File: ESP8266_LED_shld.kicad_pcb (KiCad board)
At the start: 2 copper layers, 59.1 x 52.7 mm, 28 parts, among them J1 Pwr_Dat_Out, J2 CONN_02X08, J3 CONN_DIN, J4 BARREL_JACK, J5 USB-MICROB, J6 CONN_01X06, M1 LOGIC_LEVEL_CONVERTER, T1 Test_Point_2Pads, U1 ESP-07v2, U2 AMS1117

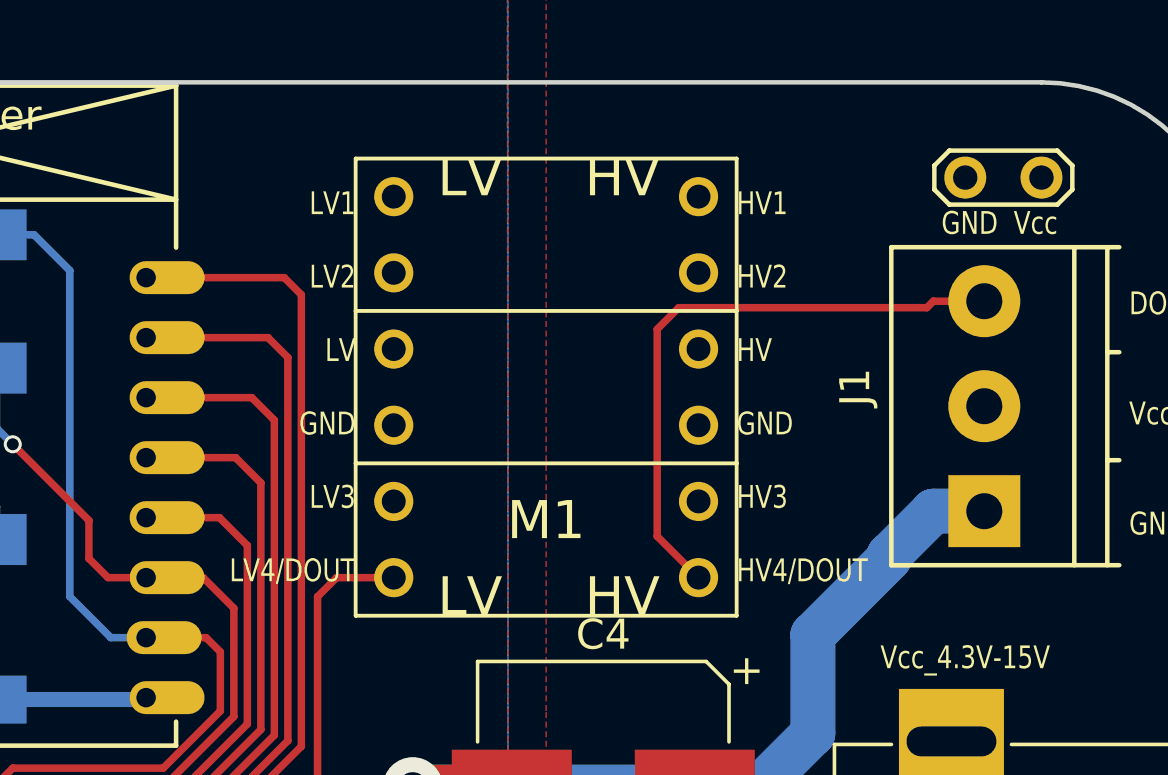
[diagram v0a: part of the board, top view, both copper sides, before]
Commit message: added resistor between DOUT and HV4 to protect data pin of LED stip and fixed some silk screen labels (positions)
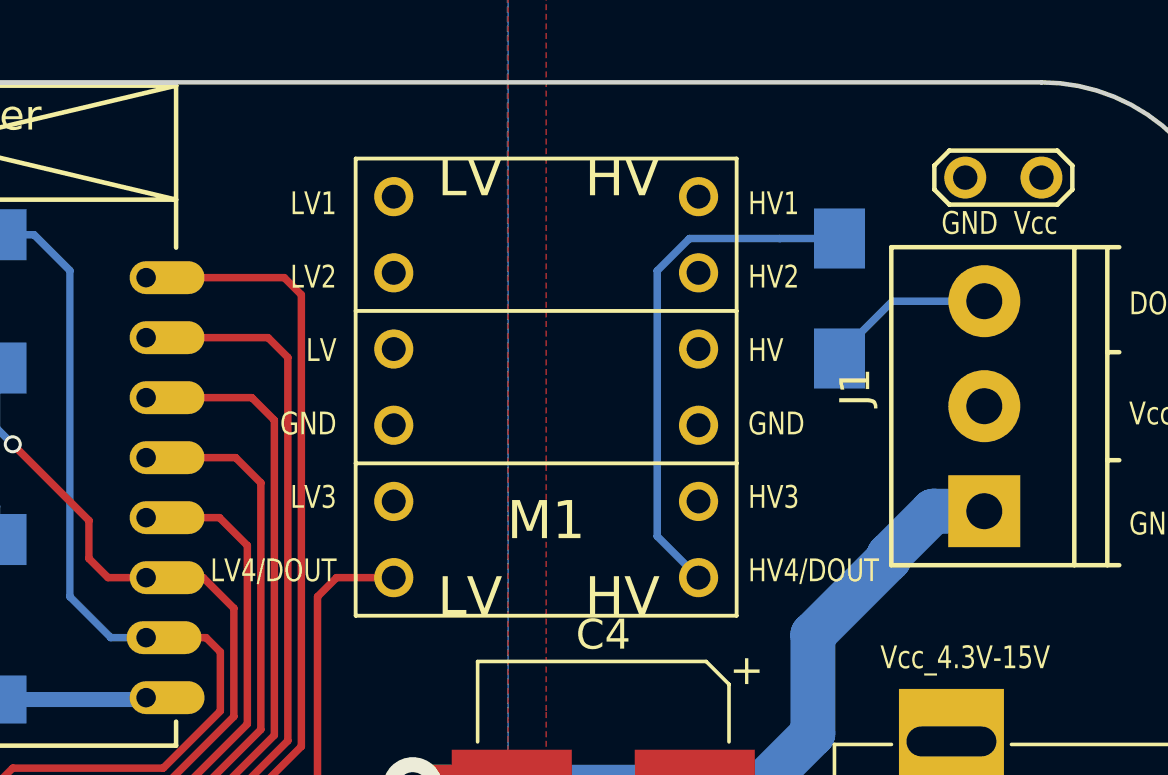
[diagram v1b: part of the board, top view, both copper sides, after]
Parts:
- added R7: 1K, Resistors_SMD:R_1206_HandSoldering, B.Cu at (204.7, 87.9)
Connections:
- M1 pad P$7: DOUT -> Net-(M1-PadP$7)
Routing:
- net Net-(M1-PadP$7): track 0.00 -> 17.3 mm
- net DOUT: track 20.5 -> 6.02 mm
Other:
- board text added: "Revision 1.1 Vcc: 4.3V-15V, 8A (PCB) +3V3: 800mA USB+DC_JACK=USB_GND_BRK USB+Vcc=NO BRK!"
- board text removed: "Revision 1.0 Vcc: 4.3V-15V, 8A (PCB) +3V3: 800mA USB+DC_JACK=USB_GND_BRK USB+Vcc=NO BRK!"
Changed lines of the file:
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@@
 (kicad_pcb (version 4) (host pcbnew 4.0.6)
   (general
-    (links 71)
-    (no_connects 3)
+    (links 72)
+    (no_connects 5)
     (area 158.674999 80.569999 217.880001 133.425001)
     (thickness 1.6)
     (drawings 27)
-    (tracks 248)
+    (tracks 250)
     (zones 0)
-    (modules 28)
-    (nets 33)
+    (modules 29)
+    (nets 34)
   )
   (page A4)
@@
   (net 31 /DTR)
   (net 32 /CTS)
+  (net 33 "Net-(M1-PadP$7)")
   (net_class Default "This is the default net class."
     (clearance 0.2)
@@
     (add_net "Net-(M1-PadP$2)")
     (add_net "Net-(M1-PadP$5)")
+    (add_net "Net-(M1-PadP$7)")
     (add_net "Net-(M1-PadP$8)")
     (add_net REST)
@@
       (net 4 DIN))
     (pad P$7 thru_hole circle (at 11.43 -1.27) (size 1.30556 1.30556) (drill 0.79756) (layers *.Cu *.Mask F.SilkS)
-      (net 3 DOUT))
+      (net 33 "Net-(M1-PadP$7)"))
     (pad P$8 thru_hole circle (at 11.43 -3.81) (size 1.30556 1.30556) (drill 0.79756) (layers *.Cu *.Mask F.SilkS)
       (net 23 "Net-(M1-PadP$8)"))
@@
       (net 25 "Net-(M1-PadP$12)"))
   )
+  (module Resistors_SMD:R_1206_HandSoldering (layer B.Cu)
+    (at 204.724 87.852 270)
+    (descr "Resistor SMD 1206, hand soldering")
+    (tags "resistor 1206")
+    (attr smd)
+    (fp_text reference R7 (at 0 1.85 270) (layer B.SilkS)
+      (effects (font (size 1 1) (thickness 0.15)) (justify mirror))
+    )
+    (fp_text value 1K (at 0 -1.9 270) (layer B.Fab)
+      (effects (font (size 1 1) (thickness 0.15)) (justify mirror))
+    )
+    (fp_text user %R (at 0 0 270) (layer B.Fab)
+      (effects (font (size 0.7 0.7) (thickness 0.105)) (justify mirror))
+    )
+    (fp_line (start -1.6 -0.8) (end -1.6 0.8) (layer B.Fab) (width 0.1))
+    (fp_line (start 1.6 -0.8) (end -1.6 -0.8) (layer B.Fab) (width 0.1))
+    (fp_line (start 1.6 0.8) (end 1.6 -0.8) (layer B.Fab) (width 0.1))
+    (fp_line (start -1.6 0.8) (end 1.6 0.8) (layer B.Fab) (width 0.1))
+    (fp_line (start 1 -1.07) (end -1 -1.07) (layer B.SilkS) (width 0.12))
+    (fp_line (start -1 1.07) (end 1 1.07) (layer B.SilkS) (width 0.12))
+    (fp_line (start -3.25 1.11) (end 3.25 1.11) (layer B.CrtYd) (width 0.05))
+    (fp_line (start -3.25 1.11) (end -3.25 -1.1) (layer B.CrtYd) (width 0.05))
+    (fp_line (start 3.25 -1.1) (end 3.25 1.11) (layer B.CrtYd) (width 0.05))
+    (fp_line (start 3.25 -1.1) (end -3.25 -1.1) (layer B.CrtYd) (width 0.05))
+    (pad 1 smd rect (at -2 0 270) (size 2 1.7) (layers B.Cu B.Paste B.Mask)
+      (net 33 "Net-(M1-PadP$7)"))
+    (pad 2 smd rect (at 2 0 270) (size 2 1.7) (layers B.Cu B.Paste B.Mask)
+      (net 3 DOUT))
+    (model ${KISYS3DMOD}/Resistors_SMD.3dshapes/R_1206.wrl
+      (at (xyz 0 0 0))
+      (scale (xyz 1 1 1))
+      (rotate (xyz 0 0 0))
+    )
+  )
   (gr_text "EN\n\n\n\nDIS" (at 163.322 124.46) (layer F.SilkS)
     (effects (font (size 0.76 0.6) (thickness 0.125)) (justify left))
@@
     (effects (font (size 0.76 0.6) (thickness 0.125)) (justify left))
   )
-  (gr_text "Revision 1.0\n\nVcc: 4.3V-15V, 8A (PCB)    +3V3: 800mA    \nUSB+DC_JACK=USB_GND_BRK\nUSB+Vcc=NO BRK!" (at 202.565 105.41) (layer B.SilkS)
+  (gr_text "Revision 1.1\n\nVcc: 4.3V-15V, 8A (PCB)    +3V3: 800mA    \nUSB+DC_JACK=USB_GND_BRK\nUSB+Vcc=NO BRK!" (at 202.565 105.41) (layer B.SilkS)
     (effects (font (size 0.9 0.9) (thickness 0.2)) (justify left mirror))
   )
@@
     (effects (font (size 0.76 0.6) (thickness 0.125)) (justify left))
   )
-  (gr_text "LV1\n\nLV2\n\nLV\n\nGND\n\nLV3\n\nLV4/DOUT" (at 188.595 90.805) (layer F.SilkS)
+  (gr_text "LV1\n\nLV2\n\nLV\n\nGND\n\nLV3\n\nLV4/DOUT" (at 187.96 90.805) (layer F.SilkS)
     (effects (font (size 0.76 0.6) (thickness 0.125)) (justify right))
   )
-  (gr_text "HV1\n\nHV2\n\nHV\n\nGND\n\nHV3\n\nHV4/DOUT" (at 201.295 90.805) (layer F.SilkS)
+  (gr_text "HV1\n\nHV2\n\nHV\n\nGND\n\nHV3\n\nHV4/DOUT" (at 201.676 90.805) (layer F.SilkS)
     (effects (font (size 0.76 0.6) (thickness 0.125)) (justify left))
   )
@@
   (segment (start 181.61 101.155) (end 181.546 101.219) (width 0.5) (layer B.Cu) (net 2))
   (segment (start 181.546 101.219) (end 176.625 101.219) (width 0.5) (layer B.Cu) (net 2))
-  (segment (start 200.025 97.155) (end 198.647219 95.777219) (width 0.25) (layer F.Cu) (net 3))
-  (segment (start 198.647219 95.777219) (end 198.647219 88.873664) (width 0.25) (layer F.Cu) (net 3))
-  (segment (start 198.647219 88.873664) (end 199.363664 88.157219) (width 0.25) (layer F.Cu) (net 3))
-  (segment (start 207.852944 87.94) (end 209.55 87.94) (width 0.25) (layer F.Cu) (net 3))
-  (segment (start 199.363664 88.157219) (end 207.635725 88.157219) (width 0.25) (layer F.Cu) (net 3))
-  (segment (start 207.635725 88.157219) (end 207.852944 87.94) (width 0.25) (layer F.Cu) (net 3))
+  (segment (start 209.55 87.94) (end 206.486 87.94) (width 0.25) (layer B.Cu) (net 3))
+  (segment (start 206.486 87.94) (end 204.724 89.702) (width 0.25) (layer B.Cu) (net 3))
+  (segment (start 204.724 89.702) (end 204.724 89.852) (width 0.25) (layer B.Cu) (net 3))
   (segment (start 209.24 87.94) (end 209.55 87.94) (width 0.25) (layer F.Cu) (net 3))
   (segment (start 189.865 97.155) (end 187.96 97.155) (width 0.25) (layer F.Cu) (net 4))
@@
   (segment (start 210.15706 125.75794) (end 210.185 125.73) (width 0.25) (layer F.Cu) (net 30))
   (segment (start 208.915 124.46) (end 208.915 123.17) (width 0.25) (layer B.Cu) (net 30))
+  (segment (start 202.735 85.852) (end 204.724 85.852) (width 0.25) (layer B.Cu) (net 33))
+  (segment (start 200.025 97.155) (end 198.647219 95.777219) (width 0.25) (layer B.Cu) (net 33))
+  (segment (start 198.647219 95.777219) (end 198.647219 86.925664) (width 0.25) (layer B.Cu) (net 33))
+  (segment (start 198.647219 86.925664) (end 199.720883 85.852) (width 0.25) (layer B.Cu) (net 33))
+  (segment (start 199.720883 85.852) (end 202.735 85.852) (width 0.25) (layer B.Cu) (net 33))
   (zone (net 0) (net_name "") (layer B.Cu) (hatch edge 0.508)
     (connect_pads (clearance 0.508))

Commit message: updated PCB design
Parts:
- D2: footprint Diodes_SMD:D_SOD-323_HandSoldering -> Diodes_SMD:D_SOD-123
- moved D2 0.13 mm to (208.8, 121.9)
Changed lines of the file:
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@@
     (thickness 1.6)
     (drawings 27)
-    (tracks 250)
+    (tracks 251)
     (zones 0)
     (modules 29)
@@
     )
   )
-  (module Diodes_SMD:D_SOD-323_HandSoldering (layer B.Cu)
-    (at 208.915 121.92 270)
-    (descr SOD-323)
-    (tags SOD-323)
-    (attr smd)
-    (fp_text reference D2 (at 0 1.85 270) (layer B.SilkS)
-      (effects (font (size 1 1) (thickness 0.15)) (justify mirror))
-    )
-    (fp_text value DIODE (at 0.1 -1.9 270) (layer B.Fab)
-      (effects (font (size 1 1) (thickness 0.15)) (justify mirror))
-    )
-    (fp_line (start -1.9 0.85) (end -1.9 -0.85) (layer B.SilkS) (width 0.12))
-    (fp_line (start 0.2 0) (end 0.45 0) (layer B.Fab) (width 0.1))
-    (fp_line (start 0.2 -0.35) (end -0.3 0) (layer B.Fab) (width 0.1))
-    (fp_line (start 0.2 0.35) (end 0.2 -0.35) (layer B.Fab) (width 0.1))
-    (fp_line (start -0.3 0) (end 0.2 0.35) (layer B.Fab) (width 0.1))
-    (fp_line (start -0.3 0) (end -0.5 0) (layer B.Fab) (width 0.1))
-    (fp_line (start -0.3 0.35) (end -0.3 -0.35) (layer B.Fab) (width 0.1))
-    (fp_line (start -0.9 -0.7) (end -0.9 0.7) (layer B.Fab) (width 0.1))
-    (fp_line (start 0.9 -0.7) (end -0.9 -0.7) (layer B.Fab) (width 0.1))
-    (fp_line (start 0.9 0.7) (end 0.9 -0.7) (layer B.Fab) (width 0.1))
-    (fp_line (start -0.9 0.7) (end 0.9 0.7) (layer B.Fab) (width 0.1))
-    (fp_line (start -2 0.95) (end 2 0.95) (layer B.CrtYd) (width 0.05))
-    (fp_line (start 2 0.95) (end 2 -0.95) (layer B.CrtYd) (width 0.05))
-    (fp_line (start -2 -0.95) (end 2 -0.95) (layer B.CrtYd) (width 0.05))
-    (fp_line (start -2 0.95) (end -2 -0.95) (layer B.CrtYd) (width 0.05))
-    (fp_line (start -1.9 -0.85) (end 1.25 -0.85) (layer B.SilkS) (width 0.12))
-    (fp_line (start -1.9 0.85) (end 1.25 0.85) (layer B.SilkS) (width 0.12))
-    (pad 1 smd rect (at -1.25 0 270) (size 1 1) (layers B.Cu B.Paste B.Mask)
-      (net 1 Vin))
-    (pad 2 smd rect (at 1.25 0 270) (size 1 1) (layers B.Cu B.Paste B.Mask)
-      (net 30 "Net-(D2-Pad2)"))
-    (model Diodes_SMD.3dshapes/D_SOD-323.wrl
-      (at (xyz 0 0 0))
-      (scale (xyz 1 1 1))
-      (rotate (xyz 0 0 180))
-    )
-  )
   (module Capacitors_SMD:CP_Elec_8x10 (layer F.Cu)
     (at 196.85 104.14 180)
@@
     )
   )
+  (module Diodes_SMD:D_SOD-123 (layer B.Cu)
+    (at 208.788 121.92 270)
+    (descr SOD-123)
+    (tags SOD-123)
+    (attr smd)
+    (fp_text reference D2 (at 0 2 270) (layer B.SilkS)
+      (effects (font (size 1 1) (thickness 0.15)) (justify mirror))
+    )
+    (fp_text value DIODE (at 0 -2.1 270) (layer B.Fab)
+      (effects (font (size 1 1) (thickness 0.15)) (justify mirror))
+    )
+    (fp_line (start -2.25 1) (end -2.25 -1) (layer B.SilkS) (width 0.12))
+    (fp_line (start 0.25 0) (end 0.75 0) (layer B.Fab) (width 0.1))
+    (fp_line (start 0.25 -0.4) (end -0.35 0) (layer B.Fab) (width 0.1))
+    (fp_line (start 0.25 0.4) (end 0.25 -0.4) (layer B.Fab) (width 0.1))
+    (fp_line (start -0.35 0) (end 0.25 0.4) (layer B.Fab) (width 0.1))
+    (fp_line (start -0.35 0) (end -0.35 -0.55) (layer B.Fab) (width 0.1))
+    (fp_line (start -0.35 0) (end -0.35 0.55) (layer B.Fab) (width 0.1))
+    (fp_line (start -0.75 0) (end -0.35 0) (layer B.Fab) (width 0.1))
+    (fp_line (start -1.4 -0.9) (end -1.4 0.9) (layer B.Fab) (width 0.1))
+    (fp_line (start 1.4 -0.9) (end -1.4 -0.9) (layer B.Fab) (width 0.1))
+    (fp_line (start 1.4 0.9) (end 1.4 -0.9) (layer B.Fab) (width 0.1))
+    (fp_line (start -1.4 0.9) (end 1.4 0.9) (layer B.Fab) (width 0.1))
+    (fp_line (start -2.35 1.15) (end 2.35 1.15) (layer B.CrtYd) (width 0.05))
+    (fp_line (start 2.35 1.15) (end 2.35 -1.15) (layer B.CrtYd) (width 0.05))
+    (fp_line (start 2.35 -1.15) (end -2.35 -1.15) (layer B.CrtYd) (width 0.05))
+    (fp_line (start -2.35 1.15) (end -2.35 -1.15) (layer B.CrtYd) (width 0.05))
+    (fp_line (start -2.25 -1) (end 1.65 -1) (layer B.SilkS) (width 0.12))
+    (fp_line (start -2.25 1) (end 1.65 1) (layer B.SilkS) (width 0.12))
+    (pad 1 smd rect (at -1.65 0 270) (size 0.9 1.2) (layers B.Cu B.Paste B.Mask)
+      (net 1 Vin))
+    (pad 2 smd rect (at 1.65 0 270) (size 0.9 1.2) (layers B.Cu B.Paste B.Mask)
+      (net 30 "Net-(D2-Pad2)"))
+    (model ${KISYS3DMOD}/Diodes_SMD.3dshapes/D_SOD-123.wrl
+      (at (xyz 0 0 0))
+      (scale (xyz 1 1 1))
+      (rotate (xyz 0 0 0))
+    )
+  )
   (gr_text "EN\n\n\n\nDIS" (at 163.322 124.46) (layer F.SilkS)
     (effects (font (size 0.76 0.6) (thickness 0.125)) (justify left))
@@
   (gr_line (start 217.805 133.35) (end 165.1 133.35) (layer Edge.Cuts) (width 0.15))
   (gr_line (start 217.805 86.995) (end 217.805 133.35) (layer Edge.Cuts) (width 0.15))
+  (segment (start 208.788 120.27) (end 208.788 118.751548) (width 0.25) (layer B.Cu) (net 1))
+  (via (at 208.915 118.624548) (size 0.6) (drill 0.4) (layers F.Cu B.Cu) (net 1))
   (segment (start 208.915 118.624548) (end 208.915 116.74856) (width 0.25) (layer F.Cu) (net 1))
-  (via (at 208.915 118.624548) (size 0.6) (drill 0.4) (layers F.Cu B.Cu) (net 1))
-  (segment (start 208.915 120.67) (end 208.915 118.624548) (width 0.25) (layer B.Cu) (net 1))
+  (segment (start 208.788 118.751548) (end 208.915 118.624548) (width 0.25) (layer B.Cu) (net 1))
   (segment (start 208.915 116.74856) (end 208.63306 116.46662) (width 1.5) (layer F.Cu) (net 1))
   (segment (start 208.63306 116.46662) (end 213.17662 116.46662) (width 0.5) (layer F.Cu) (net 1))
@@
   (segment (start 190.628 118.872) (end 190.628 123.602) (width 0.25) (layer F.Cu) (net 29))
   (segment (start 190.628 123.602) (end 190.278 123.952) (width 0.25) (layer F.Cu) (net 29))
+  (segment (start 208.788 123.57) (end 208.788 124.333) (width 0.25) (layer B.Cu) (net 30))
+  (segment (start 208.788 124.333) (end 210.185 125.73) (width 0.25) (layer B.Cu) (net 30))
   (segment (start 210.155 128.19) (end 210.155 125.76) (width 0.25) (layer F.Cu) (net 30))
   (segment (start 210.155 125.76) (end 210.185 125.73) (width 0.25) (layer F.Cu) (net 30))
-  (segment (start 210.185 125.73) (end 208.915 124.46) (width 0.25) (layer B.Cu) (net 30))
   (via (at 210.185 125.73) (size 0.6) (drill 0.4) (layers F.Cu B.Cu) (net 30))
   (segment (start 210.15706 125.75794) (end 210.185 125.73) (width 0.25) (layer F.Cu) (net 30))
-  (segment (start 208.915 124.46) (end 208.915 123.17) (width 0.25) (layer B.Cu) (net 30))
   (segment (start 202.735 85.852) (end 204.724 85.852) (width 0.25) (layer B.Cu) (net 33))
   (segment (start 200.025 97.155) (end 198.647219 95.777219) (width 0.25) (layer B.Cu) (net 33))

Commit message: work started on rev2 [wip]
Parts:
- removed M1: LOGIC_LEVEL_CONVERTER, FixedComponents:LOGIC_LEVEL_CONVERTER-revision2
- added Q1: BSS138, TO_SOT_Packages_SMD:SOT-23, F.Cu at (200.4, 87.1)
- added Q2: BSS138, TO_SOT_Packages_SMD:SOT-23, F.Cu at (192.3, 87.1)
- added R10: 10K, Resistors_SMD:R_1206_HandSoldering, F.Cu at (192.3, 83.3)
- added R8: 10K, Resistors_SMD:R_1206_HandSoldering, F.Cu at (200.4, 91.2)
- added R9: 10K, Resistors_SMD:R_1206_HandSoldering, F.Cu at (200.4, 83.3)
- C1: moved to B.Cu
- C3: value 220uF -> 470uF; footprint Capacitors_SMD:C_1206_HandSoldering -> Capacitors_SMD:CP_Elec_8x10; moved to F.Cu
- J1: footprint Connectors_Terminal_Blocks:TerminalBlock_Pheonix_PT-3.5mm_3pol -> Connectors_Terminal_Blocks:TerminalBlock_Pheonix_MKDS1.5-3pol
- J4: footprint Connectors:BARREL_JACK -> BARREL_JACK-revision2
- R6: value 65 -> 470
- R7: value 1K -> 10K; moved to F.Cu
- U2: footprint SparkFun-PowerIC:V-REG_DPACK-revision2 -> TO_SOT_Packages_SMD:SOT-223-3Lead_TabPin2
- moved MH1 43.7 mm to (162.6, 85.1)
- moved C1 37.1 mm to (174.6, 101.2)
- moved MH2 27.7 mm to (162.8, 129.3)
- moved J3 27.3 mm to (186.7, 86.1), turned to 0 degrees
- moved JP1 25.4 mm to (161.9, 96.5), turned to 180 degrees
- moved T1 19.3 mm to (199.6, 68.6)
- moved D2 17.4 mm to (225.6, 126.5)
- moved J5 17.1 mm to (227.3, 135.9)
- moved C2 14.9 mm to (200.4, 126.0), turned to 0 degrees
- moved C3 14.6 mm to (189.2, 100.3), turned to 270 degrees
- moved R7 12.9 mm to (192.3, 91.2), turned to 0 degrees
- moved U2 12.3 mm to (193.7, 111.8)
- moved R1 12.2 mm to (162.6, 120.4)
- moved R4 11.7 mm to (175.8, 120.4)
- moved LED1 11.3 mm to (190.5, 130.0), turned to 180 degrees
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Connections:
- C2 pad 1: Vin -> VCC
- C4 pad 1: Vin -> VCC
- D2 pad 1: Vin -> VCC
- J1 pad 2: Vin -> VCC
- J1 pad 3: DOUT -> HV1
- J2 pad 1: TXD -> GPIO15
- J2 pad 10: +3V3 -> ADC
- J2 pad 11: GPIO14 -> CH_PD
- J2 pad 12: GPIO12 -> GPIO16
- J2 pad 13: CH_PD -> GPIO14
- J2 pad 14: GPIO16 -> GPIO12
- J2 pad 15: REST -> GPIO13
- J2 pad 16: ADC -> +3V3
- J2 pad 2: RXD -> GND
- J2 pad 3: GPIO5 -> GPIO0
- J2 pad 4: GPIO4 -> GPIO2
- J2 pad 5: GPIO0 -> GPIO5
- J2 pad 6: GPIO2 -> GPIO4
- J2 pad 7: GPIO15 -> TXD
- J2 pad 8: GND -> RXD
- J2 pad 9: GPIO13 -> REST
- J3 pad 1: DIN -> LV1
- J3 pad 2: DIN -> LV2
- J4 pad 1: Vin -> VCC
- R7 pad 1: Net-(M1-PadP$7) -> +3V3
- R7 pad 2: DOUT -> LV2
- U2 pad 3: Vin -> VCC
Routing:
- net GND: track 64.8 -> 20.2 mm, vias 4 -> 3
- net +3V3: track 34.3 -> 71.5 mm
- net GNDBREAK: track 33.2 -> 0.00 mm, vias 2 -> 0
- net LV1: track 0.00 -> 22.0 mm, vias 0 -> 1
- net DIN: track 21.1 -> 0.00 mm
- net HV1: track 0.00 -> 19.9 mm
- net Vin: track 19.2 -> 0.00 mm, vias 1 -> 0
- net GPIO15: track 36.8 -> 18.5 mm
- net Net-(M1-PadP$7): track 17.3 -> 0.00 mm
- net CH_PD: track 43.9 -> 27.2 mm
- net LV2: track 0.00 -> 12.5 mm, vias 0 -> 1
- net GPIO0: track 40.7 -> 28.2 mm
- net GPIO16: track 41.3 -> 29.1 mm
- net VCC: track 0.00 -> 11.8 mm, vias 0 -> 2
- net GPIO2: track 34.1 -> 24.8 mm, vias 1 -> 0
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- added copper zone on F.Cu, net VCC
- removed copper zone on F.Cu, net Vin
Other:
- board text added: "3V3 GP12 GP16 ADC RXD GP4 GP2 GND"
- board text added: "GND"
- board text added: "GP13 GP14 CH_PD REST TXD GP5 GP0 GP15"
- board text added: "LV1 LV2"
- board text added: "Vcc"
- board text removed: "ADC GPIO16 GPIO12 3V3 GND GPIO2 GPIO4 RXD"
- board text removed: "DIN DIN"
- board text removed: "RST CH_PD GPIO14 GPIO13 GPIO15 GPIO0 GPIO5 TXD"

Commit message: changed usb micro b to usb mini b & added CH340G IC. some changes to PCB.
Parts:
- added MH2: MountingHole_3.2mm_M3, Mounting_Holes:MountingHole_3.2mm_M3, F.Cu at (213.9, 129.2)
- D2: moved to F.Cu
- J5: value USB-MICROB -> USB_B; footprint FixedComponents:USB_Micro-B-revision2 -> Connectors:USB_Mini-B
- moved T1 43.4 mm to (204.2, 111.8), turned to 270 degrees
- moved J5 24.7 mm to (212.9, 115.8), turned to 180 degrees
- moved D2 22.2 mm to (204.2, 120.4), turned to 0 degrees
- moved C2 13.6 mm to (200.7, 112.4), turned to 90 degrees
- moved T1 2.54 mm to (160.9, 108.7)
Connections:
- D2 pad 2: Net-(D2-Pad2) -> /VBUS
- T1 pad 1: Vin -> VCC
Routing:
- net VCC: track 11.8 -> 62.4 mm, vias 2 -> 3
- net GNDBREAK: track 0.00 -> 22.7 mm, vias 0 -> 1
- net GND: track 20.2 -> 32.1 mm, vias 3 -> 4
- net +3V3: track 71.5 -> 77.8 mm
- net /VBUS: track 0.00 -> 5.64 mm
- net HV1: track 19.9 -> 18.7 mm, vias 0 -> 1
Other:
- outline, holes or cut-outs redrawn
- board text added: "LV1 <-> HV1 LV2 <-> HV2"
- board text removed: "HV1 HV2 HV GND HV3 HV4/DOUT"
- board text removed: "LV1 LV2 LV GND LV3 LV4/DOUT"
